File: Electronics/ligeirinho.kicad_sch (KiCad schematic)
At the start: 19 parts, among them J1 VS1838B, J10 ponte H, J11 ponte H ld motores, J12 MPU6050, J2 motor B, J3 motor A, J4 ESP32 esq, J5 VL53L0X 1, J6 VL53L0X 2, J7 VL53L0X 3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

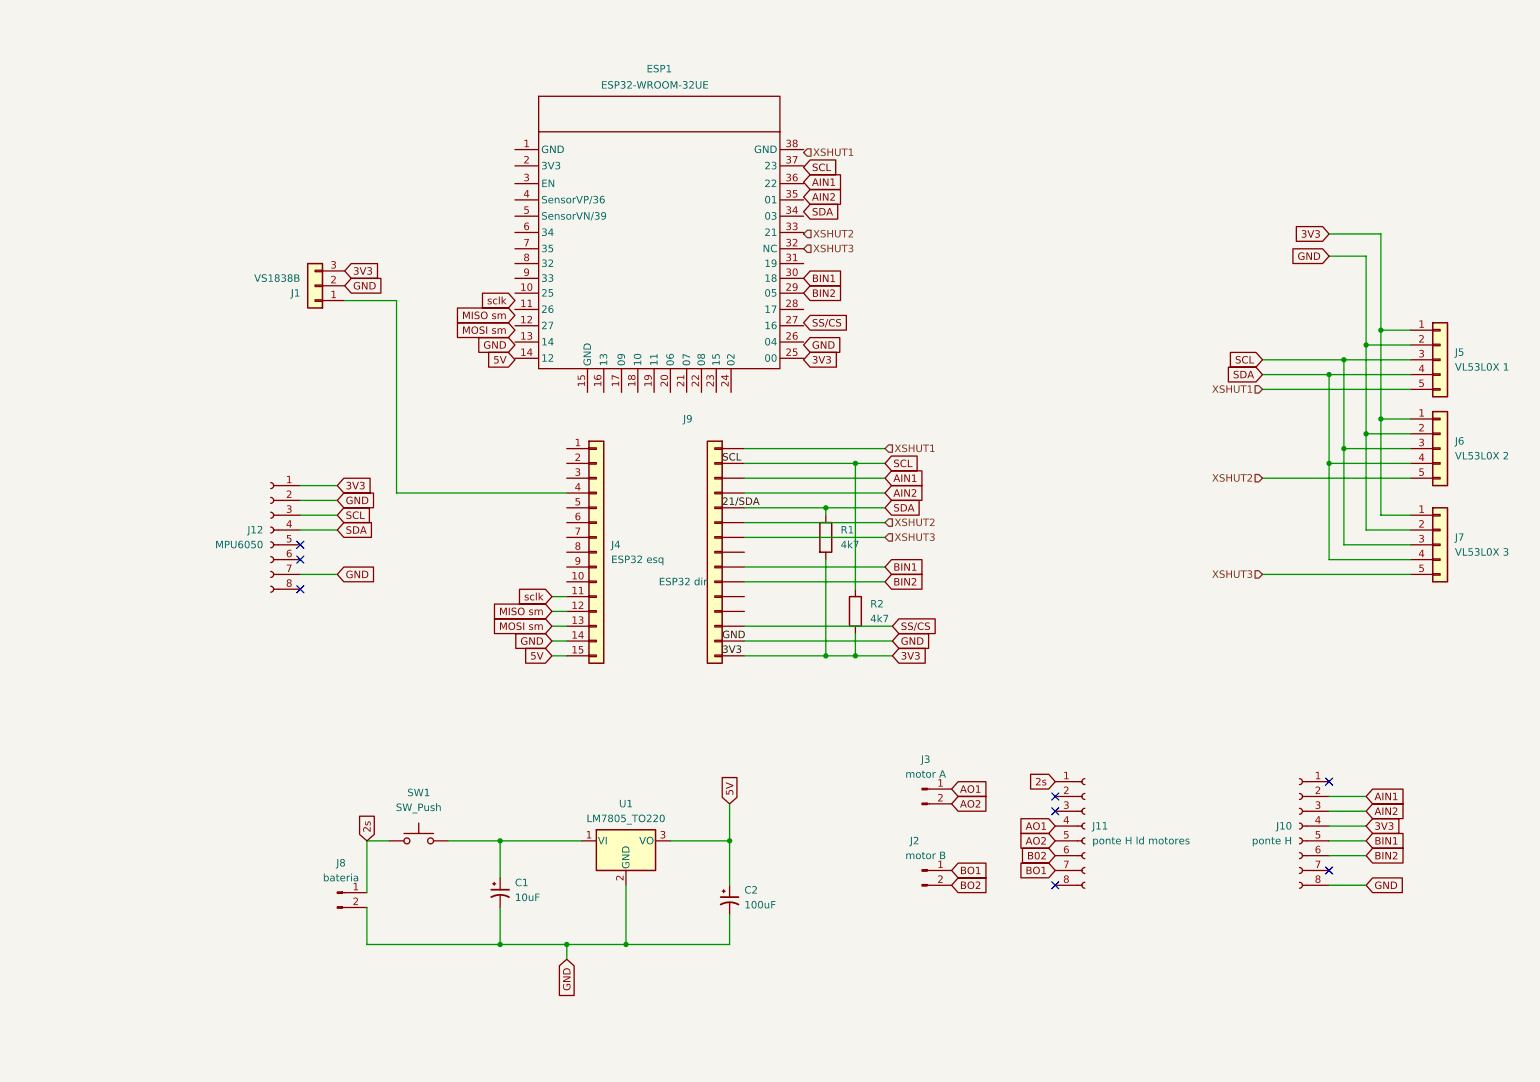
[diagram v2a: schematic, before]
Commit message: shore: update PCB repository
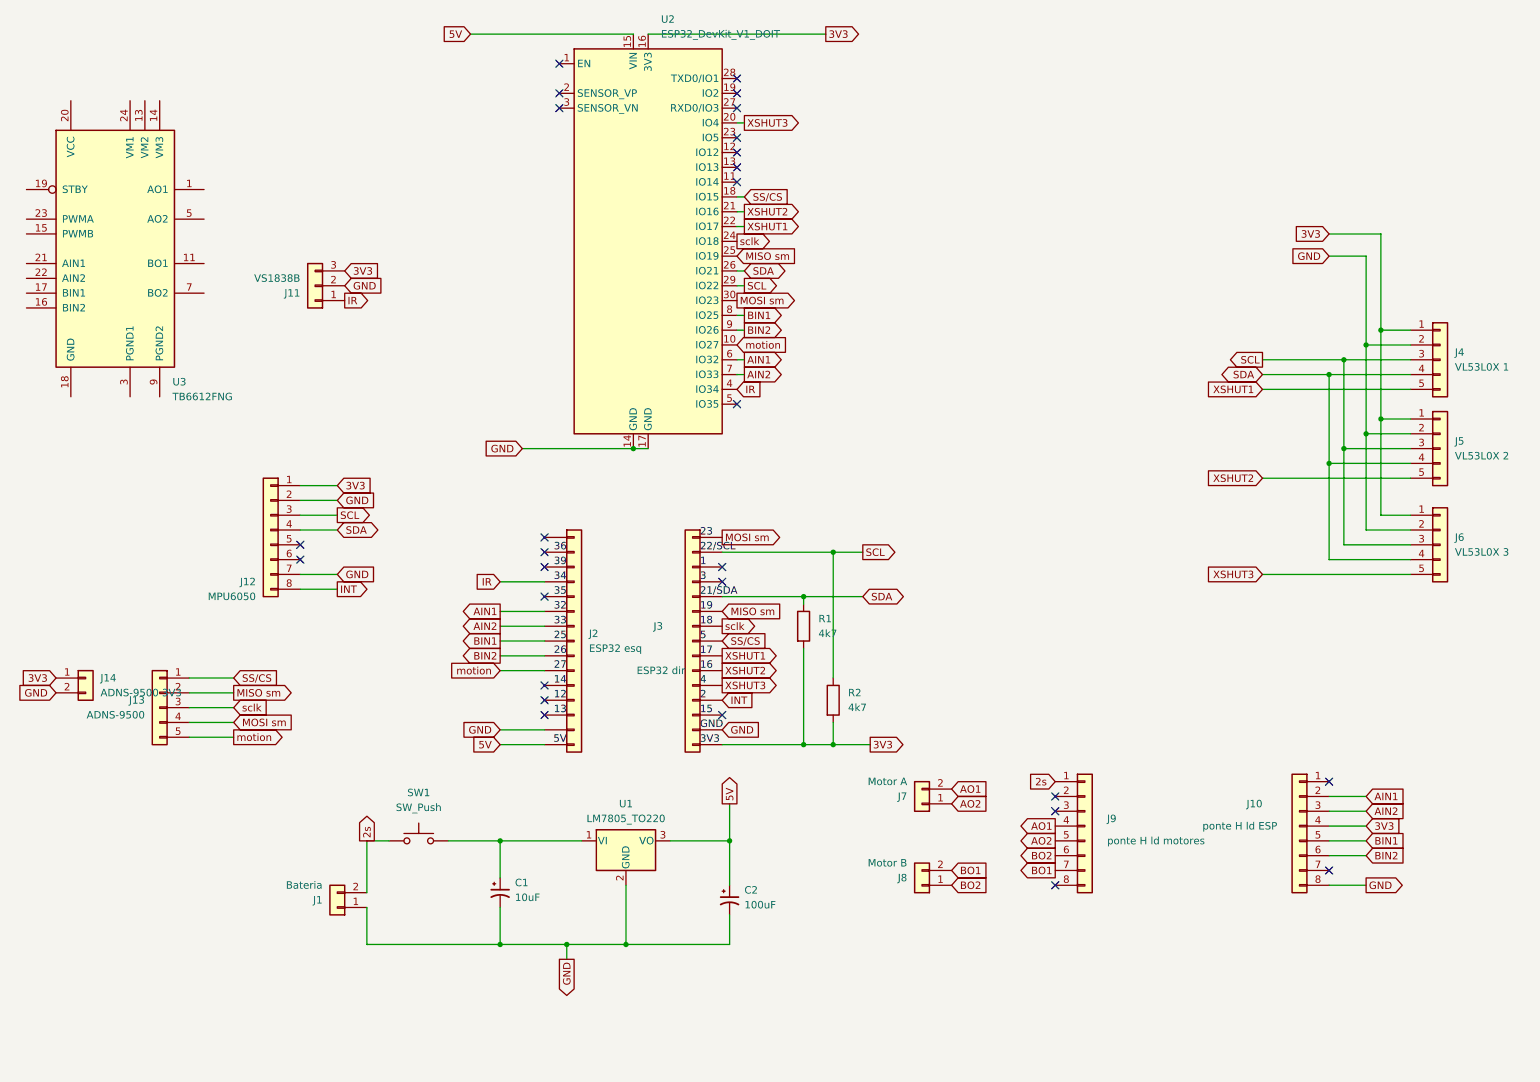
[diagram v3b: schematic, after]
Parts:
- removed ESP1: ESP32-WROOM­32UE, RF_Module:ESP32-WROOM-32, symbol espSMD:ESP32-WROOM­32UE
- removed J10: ponte H, symbol Connector:Conn_01x08_Socket
- removed J11: ponte H ld motores, symbol Connector:Conn_01x08_Socket
- removed J12: MPU6050, symbol Connector:Conn_01x08_Socket
- removed J2: motor B, symbol Connector:Conn_01x02_Pin
- removed J3: motor A, symbol Connector:Conn_01x02_Pin
- removed J8: bateria, symbol Connector:Conn_01x02_Pin
- added J1: Bateria, Connector_JST:JST_PH_B2B-PH-K_1x02_P2.00mm_Vertical, symbol Connector_Generic:Conn_01x03
- added J10: ponte H ld ESP, Connector_PinSocket_2.54mm:PinSocket_1x08_P2.54mm_Vertical, symbol Connector_Generic:Conn_01x15
- added J12: MPU6050, Connector_PinSocket_2.54mm:PinSocket_1x08_P2.54mm_Vertical, symbol Connector_Generic:Conn_01x15
- added J13: ADNS-9500, Connector_JST:JST_XH_S5B-XH-A_1x05_P2.50mm_Horizontal, symbol Connector_Generic:Conn_01x07
- added J14: ADNS-9500 3V3, Connector_JST:JST_XH_S2B-XH-A_1x02_P2.50mm_Horizontal, symbol Connector_Generic:Conn_01x02
- added J7: Motor A, Connector_JST:JST_XH_B2B-XH-AM_1x02_P2.50mm_Vertical, symbol Connector_Generic:Conn_01x03
- added J8: Motor B, Connector_JST:JST_XH_B2B-XH-AM_1x02_P2.50mm_Vertical, symbol Connector_Generic:Conn_01x03
- added J9: ponte H ld motores, Connector_PinSocket_2.54mm:PinSocket_1x08_P2.54mm_Vertical, symbol Connector_Generic:Conn_01x15
- added U2: ESP32_DevKit_V1_DOIT, KIKAD bibliotecas:esp32_devkit_v1_doit, symbol esp32_devkit_v1_doit:ESP32_DevKit_V1_DOIT
- added U3: TB6612FNG, KIKAD bibliotecas:TB6612FNG_Dual_Motor_Driver_Carrier, symbol Driver_Motor:TB6612FNG
- C1: footprint (none) -> Capacitor_THT:CP_Radial_D5.0mm_P2.50mm
- C2: footprint (none) -> Capacitor_THT:CP_Radial_D6.3mm_P2.50mm
- J11: renamed from J1; footprint (none) -> Connector_PinHeader_2.54mm:PinHeader_1x03_P2.54mm_Vertical
- J2: renamed from J4; footprint RF_Module:ESP32-WROOM-32 -> Connector_PinSocket_2.54mm:PinSocket_1x15_P2.54mm_Vertical
- J3: renamed from J9; footprint RF_Module:ESP32-WROOM-32 -> Connector_PinSocket_2.54mm:PinSocket_1x15_P2.54mm_Vertical
- J4: renamed from J5; footprint (none) -> Connector_JST:JST_XH_B5B-XH-AM_1x05_P2.50mm_Vertical
- J5: renamed from J6; footprint (none) -> Connector_JST:JST_XH_B5B-XH-AM_1x05_P2.50mm_Vertical
- J6: renamed from J7; footprint (none) -> Connector_JST:JST_XH_B5B-XH-AM_1x05_P2.50mm_Vertical
- R1, R2: footprint (none) -> Resistor_THT:R_Axial_DIN0207_L6.3mm_D2.5mm_P10.16mm_Horizontal
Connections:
- net 2s: now also J1.2 (Pin_2), J9.1 (Pin_1)
- net 3V3: now also J10.4 (Pin_4), J12.1 (Pin_1), J14.1 (Pin_1), U2.16 (3V3)
- net 5V: now also U2.15 (VIN)
- net AIN1: now also J2.6 (Pin_6), J10.2 (Pin_2), U2.6 (IO32); no longer J3.3 (Pin_3)
- net AIN2: now also J2.7 (Pin_7), J10.3 (Pin_3), U2.7 (IO33); no longer J3.4 (Pin_4)
- net AO1: now also J7.2 (Pin_2), J9.4 (Pin_4)
- net AO2: now also J7.1 (Pin_1), J9.5 (Pin_5)
- net BIN1: now also J2.8 (Pin_8), J10.5 (Pin_5), U2.8 (IO25); no longer J3.9 (Pin_9)
- net BIN2: now also J2.9 (Pin_9), J10.6 (Pin_6), U2.9 (IO26); no longer J3.10 (Pin_10)
- net BO1: now also J8.2 (Pin_2), J9.7 (Pin_7)
- net BO2: now also J8.1 (Pin_1), J9.6 (Pin_6)
- net GND: now also J1.1 (Pin_1), J10.8 (Pin_8), J12.2 (Pin_2), J12.7 (Pin_7), J14.2 (Pin_2), U2.14 (GND), U2.17 (GND)
- net MISO sm: now also J3.6 (Pin_6), J13.2 (Pin_2), U2.25 (IO19); no longer J2.12 (Pin_12)
- net MOSI sm: now also J3.1 (Pin_1), J13.4 (Pin_4), U2.30 (IO23); no longer J2.13 (Pin_13)
- net SCL: now also J12.3 (Pin_3), U2.29 (IO22)
- net SDA: now also J12.4 (Pin_4), U2.26 (IO21)
- net SS/CS: now also J3.8 (Pin_8), J13.1 (Pin_1), U2.18 (IO15); no longer J3.13 (Pin_13)
- net XSHUT1: now also J3.9 (Pin_9), U2.22 (IO17); no longer J3.1 (Pin_1)
- net XSHUT2: now also J3.10 (Pin_10), U2.21 (IO16); no longer J3.6 (Pin_6)
- net XSHUT3: now also J3.11 (Pin_11), U2.20 (IO4); no longer J3.7 (Pin_7)
- net sclk: now also J3.7 (Pin_7), J13.3 (Pin_3), U2.24 (IO18); no longer J2.11 (Pin_11)
- net INT: now reaches J3.12 (Pin_12)
- net INT: now also J12.8 (Pin_8)
- net IR: now reaches J11.1 (Pin_1), J2.4 (Pin_4)
- net IR: now also U2.4 (IO34)
- net motion: now reaches J2.10 (Pin_10)
- net motion: now also J13.5 (Pin_5), U2.10 (IO27)
- new net: U3.1 (AO1), U3.2 (AO1)
- new net: U3.10 (PGND2), U3.9 (PGND2)
- new net: U3.11 (BO1), U3.12 (BO1)
- new net: U3.3 (PGND1), U3.4 (PGND1)
- new net: U3.5 (AO2), U3.6 (AO2)
- new net: U3.7 (BO2), U3.8 (BO2)
- no-connect marks 8 -> 28
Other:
- moved on the sheet: J3, R1, R2

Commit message: add: AMS1117 to 3v3 regulator
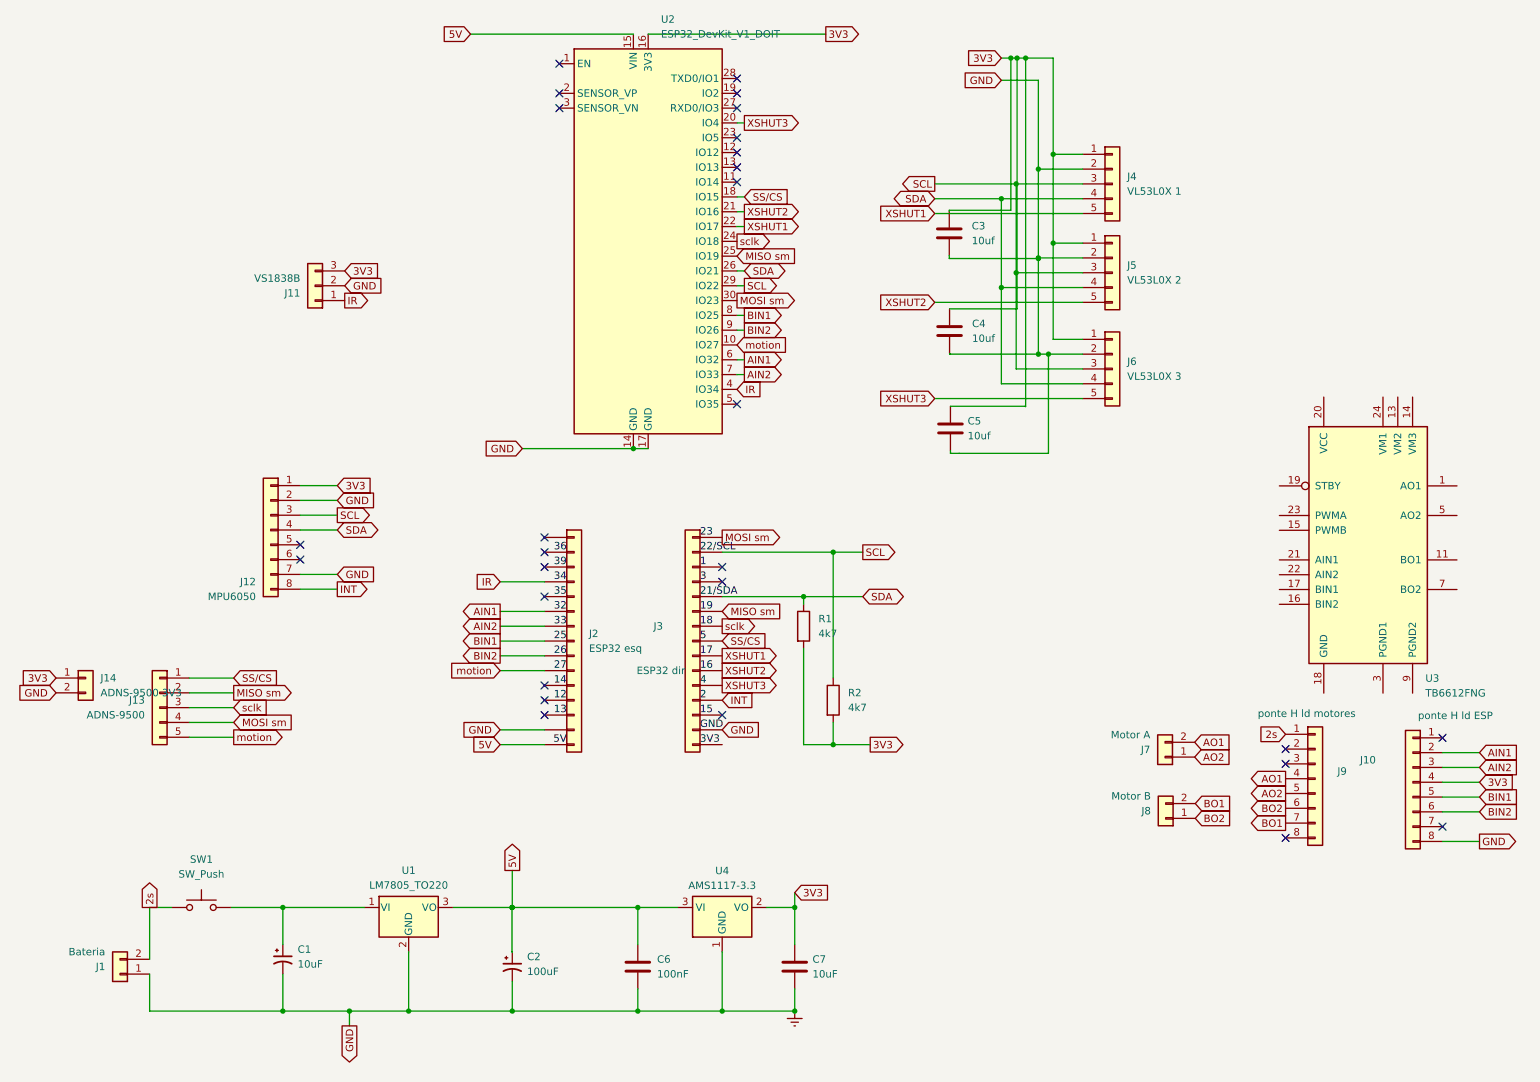
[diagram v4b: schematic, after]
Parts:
- added C3, C4, C5: 10uf, Capacitor_SMD:C_0805_2012Metric_Pad1.18x1.45mm_HandSolder, symbol Device:C
- added C6: 100nF, Capacitor_SMD:C_0805_2012Metric_Pad1.18x1.45mm_HandSolder, symbol Device:C
- added C7: 10uF, Capacitor_SMD:C_0805_2012Metric_Pad1.18x1.45mm_HandSolder, symbol Device:C
- added U4: AMS1117-3.3, Package_TO_SOT_SMD:SOT-223-3_TabPin2, symbol Regulator_Linear:AMS1117-3.3
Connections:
- net 3V3: now also C3.1, C4.1, C5.1, C7.1, U4.2 (VO); no longer J3.15 (Pin_15)
- net 5V: now also C6.1, U4.3 (VI)
- net GND renamed GNDREF
- net GNDREF: now also C3.2, C4.2, C5.2, C6.2, C7.2, U4.1 (GND)
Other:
- moved on the sheet: C1, C2, J1, J10, J4, J5, J6, J7, J8, J9, SW1, U1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
